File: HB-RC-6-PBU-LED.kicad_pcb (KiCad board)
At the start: 2 copper layers, 50 x 50 mm, 44 parts, among them J1 Maincon, J2 ISP, J3 FTDI, Q1 IRLML9301, SW1 Config, SW2 BTN1, SW3 BTN2, SW4 BTN3, SW5 BTN4, SW6 BTN5, SW7 BTN6, U1 ATmega644A-AU, U2 CC1101, U3 SN74LVC1T45DBV

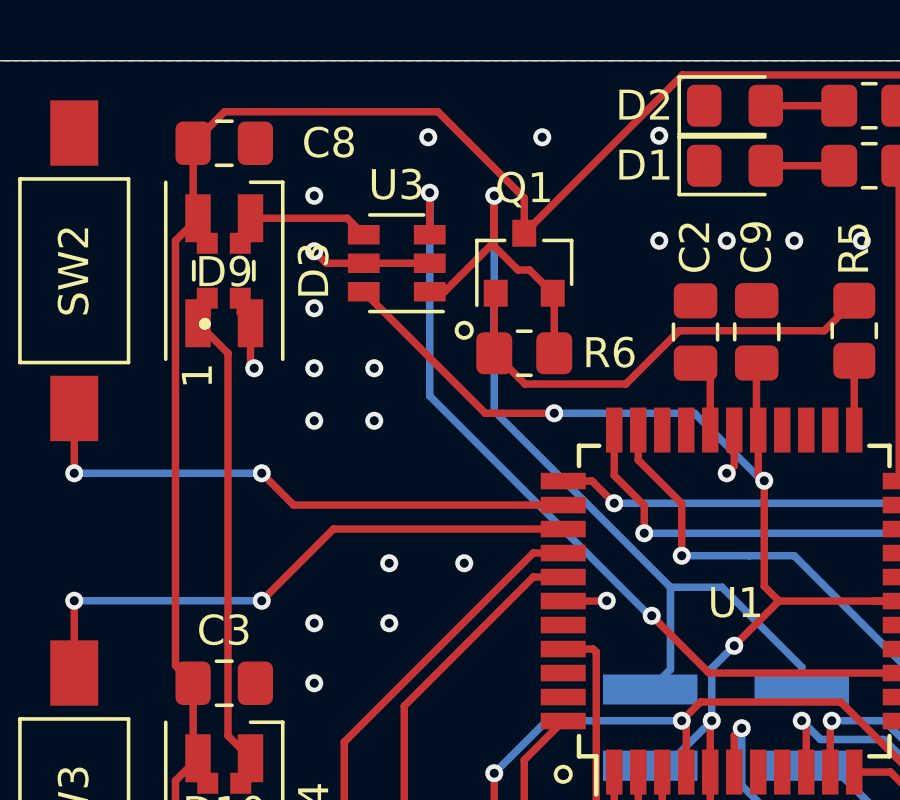
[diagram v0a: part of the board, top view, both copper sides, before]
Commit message: Bugfix on Transceiver PIN A B
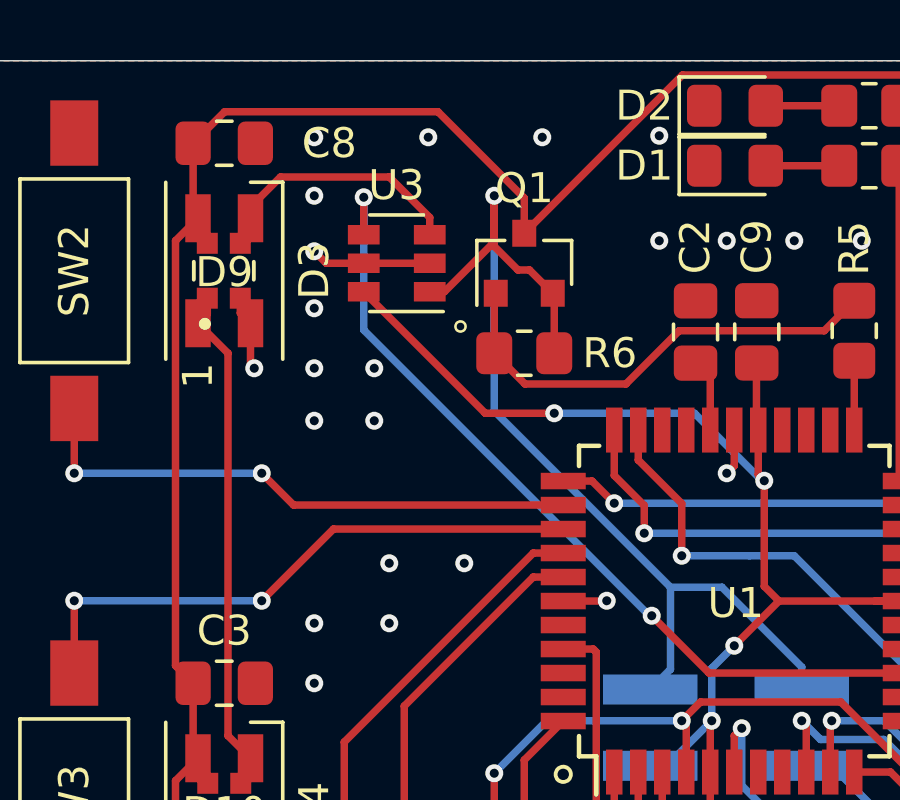
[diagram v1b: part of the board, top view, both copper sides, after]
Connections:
- U3 pad 3: /WS2812B_LED_3V3_Lvl -> /WS2812B_LED_5V_Lvl
- U3 pad 4: /WS2812B_LED_5V_Lvl -> /WS2812B_LED_3V3_Lvl
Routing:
- net /WS2812B_LED_5V_Lvl: track 5.26 -> 8.87 mm
- net /WS2812B_LED_3V3_Lvl: track 27.9 -> 28.7 mm
- net GND: vias 36 -> 37
